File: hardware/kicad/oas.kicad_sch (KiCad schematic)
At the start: 0 parts

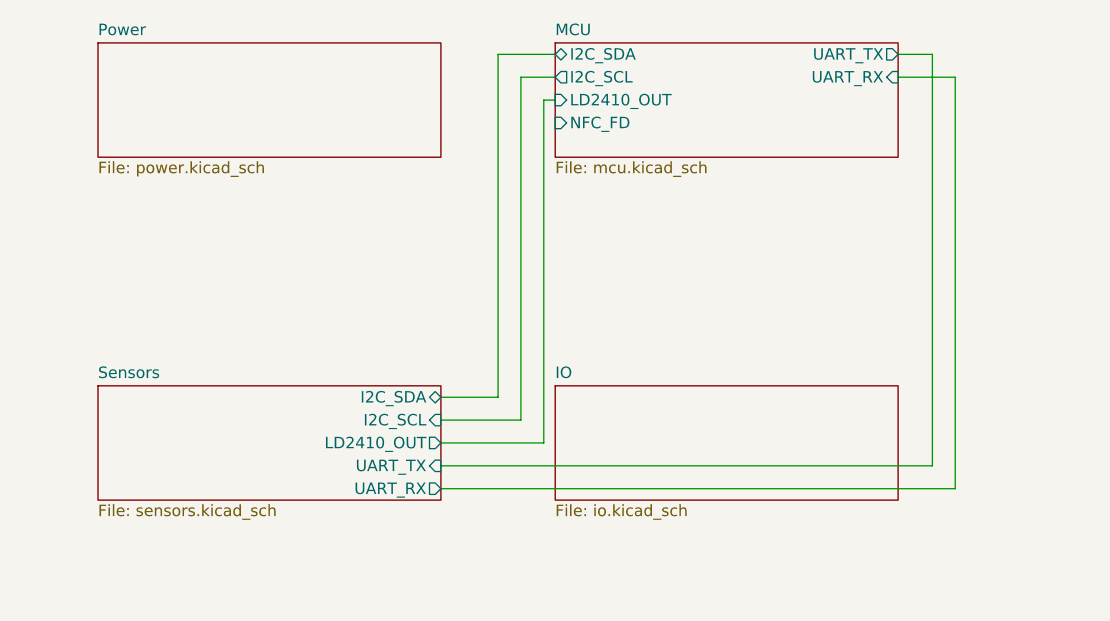
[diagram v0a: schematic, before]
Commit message: kicad: chunk #5c - MIKROE-2462 NFC Tag 2 Click (U4 + C12)
Final sensors-sub-sheet chunk: the NFC tag connection. Closes the
last expected ERC hier-label warning (NFC_FD).

Architecture change vs the v0.6 plan (a discrete NXP NT3H2x11 SMD +
custom PCB-trace NFC antenna): we instead host the NFC tag on a
MikroElektronika "NFC Tag 2 Click" (MIKROE-2462) -- NT3H2111 NTAG
I2C plus + onboard pre-tuned PCB antenna + mikroBUS 2x8 male header.
The Click board plugs into a 2x8 female pin socket on the OAS PCB
(P2.54 mm). Pre-tuned antenna eliminates the NXP AN11203 antenna-
design sub-project entirely; mikroBUS form factor is easy to source
(TME / Distrelec / Farnell / RS in the EU) and easy to swap or
remove for service via the pin-only mating.

Research summary (May 2026) drove the choice:
- MIKROE-2462 (NT3H2111 + antenna, mikroBUS, ~12-15 USD): selected.
- MIKROE-3659 (ST25DV16K, mikroBUS): strong runner-up; better EU
  stock but less DIY/ESPHome precedent.
- M5Stack U216, DFRobot DFR0231: rejected -- both are NFC readers
  (ST25R3916, PN532), not writeable tags.
- Adafruit NTAG I2C breakout: confirmed non-existent in catalog.
- Generic AliExpress NT3H2x11 breakouts: no citable listing meeting
  the Module Identification rule.

Schematic content (sensors.kicad_sch):
  U4 = Connector_Generic:Conn_02x08_Top_Bottom (placeholder for the
       mikroBUS socket; PCB footprint = 2x8 female pin socket P2.54
       mm, lands in chunk #7). The Top_Bottom variant of Conn_02x08
       has pins 1-8 down the LEFT column and 9-16 down the RIGHT
       column, exactly matching the mikroBUS pin-numbering convention.
       Only 6 pins are connected (the other 10 get no_connect markers):
         mikroBUS  7 (+3.3V) -> +3V3 power flag
         mikroBUS  8 (GND)   -> GND power flag
         mikroBUS 10 (INT)   -> NFC_FD hier label (output direction)
                                going to MCU GPIO 3
         mikroBUS 13 (SCL)   -> I2C_SCL hier label
         mikroBUS 14 (SDA)   -> I2C_SDA 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
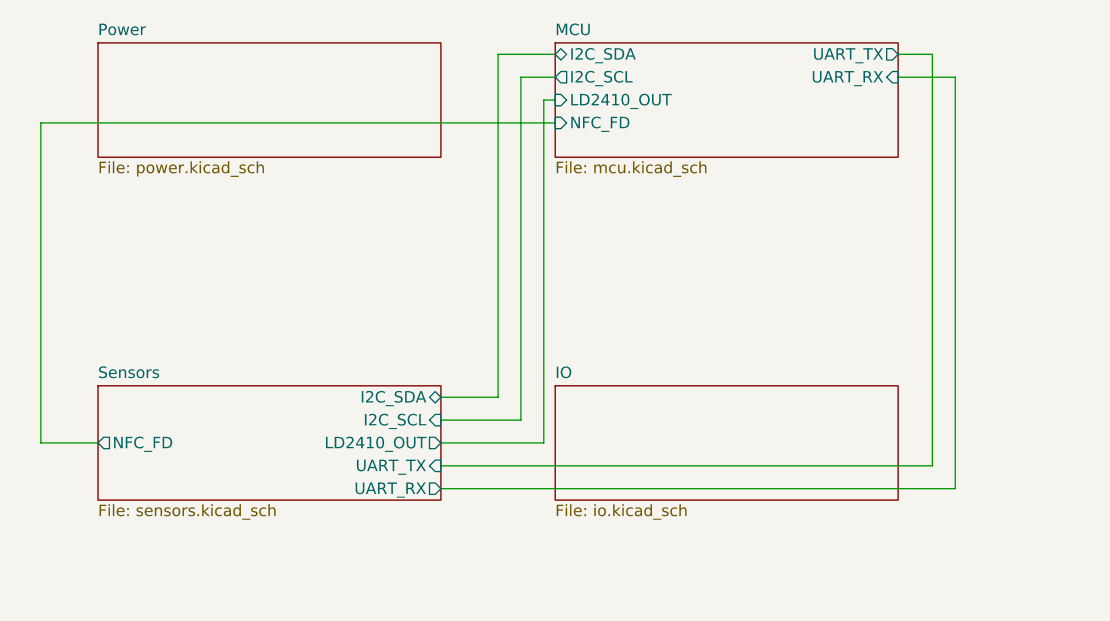
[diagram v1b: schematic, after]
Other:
- sheet Sensors ports: added NFC_FD; removed none
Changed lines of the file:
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@@
+			)
+		)
+		(pin "NFC_FD" output
+			(at 50.8 95.25 180)
+			(effects
+				(font
+					(size 1.27 1.27)
+				)
+				(justify right)
 			)
 		)
@@
 	)
 	(stroke
+		(width 0)
+		(type default)
+	)
+)
+(wire
+	(pts
+		(xy 50.8 95.25) (xy 44.45 95.25)
+	)
+	(stroke
+		(width 0)
+		(type default)
+	)
+)
+(wire
+	(pts
+		(xy 44.45 95.25) (xy 44.45 59.69)
+	)
+	(stroke
+		(width 0)
+		(type default)
+	)
+)
+(wire
+	(pts
+		(xy 44.45 59.69) (xy 101.6 59.69)
+	)
+	(stroke

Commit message: kicad+docs: v0.16 - AQI status LED ring (12 x SK6812-SIDE) + resolve OPEN ISSUE #2
Builds the side-emit RGB halo around the central cable hole: 12 SK6812 SIDE-A
LEDs on a Ø22 mm pitch circle (PCB origin = cable hole centre), each oriented
to emit radially OUTWARD into the AK-N-94 perforated cover. Per
hardware/components/_research-led-diffuse-ring.md the side-emit geometry
eliminates the "dot through perforation" problem at the structural level —
the cover never sees the die in line-of-sight.

Pinout verified twice (Normand SK6812 SIDE-A 2018 rev 01 + OPSCO SK6812
SIDE-A-001 2021 rev A/1, both via WebFetch + pdftotext): 1=DIN, 2=VDD,
3=DOUT, 4=GND. This differs from KiCad's stock LED:SK6812 symbol (which
is the PLCC4 5050 variant with 1=VSS/2=DIN/3=VDD/4=DOUT) — OAS ships its
own OAS:SK6812-SIDE symbol and oas:SK6812-SIDE footprint to avoid that
pitfall. Full part spec in hardware/components/sk6812-side.md.

Schematic additions (sensors.kicad_sch):
- 12 × D11..D22 OAS:SK6812-SIDE instances + 12 × C20..C31 Device:C 100 nF
  decoupling caps, vertical stack at X=40.64 with 25.4 mm row pitch.
- Daisy chain DIN→DOUT via 5-segment L-routes that bypass each LED body
  (avoids the spurious DIN↔DOUT short that a horizontal pass-through
  wire would create).
- D11 DIN driven from the new WS2812_DIN hierarchical label.
- D22 DOUT terminated with a no_connect.

Schematic / inter-sheet plumbing:
- mcu.kicad_sch: GPIO 8 (J1.9) moved from no-connect to signal pins.
  New WS2812_DIN hier label on the LEFT edge at the GPIO 8 pin row.
- SUBSHEET_PINS adds WS2812_DIN on the MCU and Sensors LEFT edges.
- Root sheet adds an inter-sheet wire at X = 41.91 (one grid step west
  of the existing NFC_FD vertical) joining the two new sheet pins.

PCB additions (oas.kicad_pcb):
- 12 × SK6812-SIDE footprints placed at θ = 0°..330° (30° steps) on the
  Ø22 mm pitch circle, each rotated to (270 - θ) so its body-local -Y
  (emission face) points radially outward.
- 12 × 100 nF 0402 caps, placed rad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
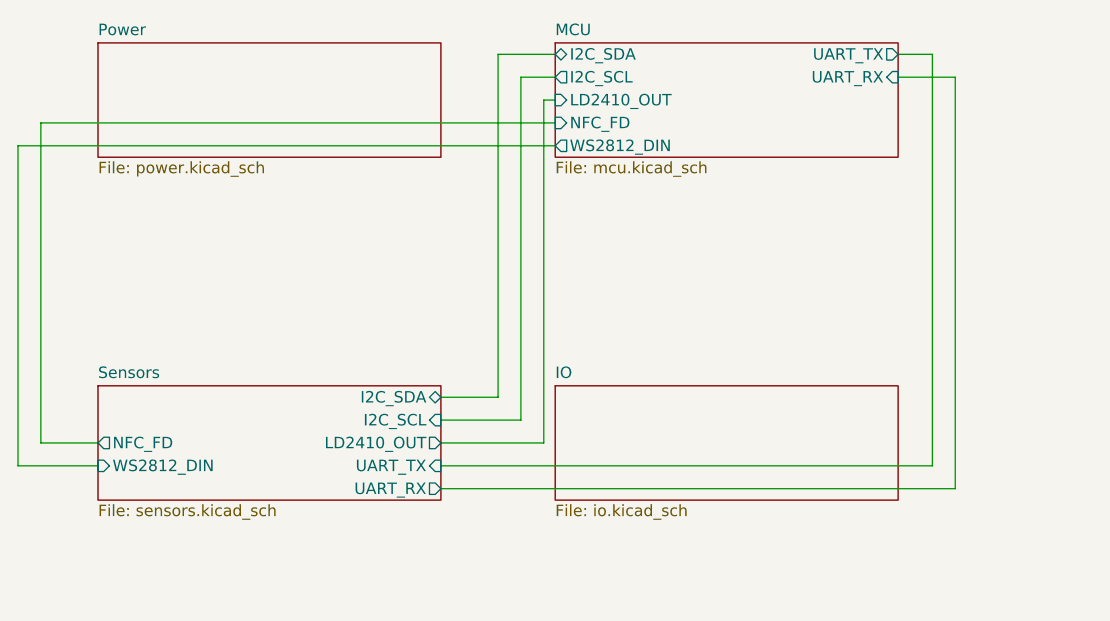
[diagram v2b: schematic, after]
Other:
- sheet MCU ports: added WS2812_DIN; removed none
- sheet Sensors ports: added WS2812_DIN; removed none
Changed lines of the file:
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@@
+			)
+		)
+		(pin "WS2812_DIN" output
+			(at 101.6 62.23 180)
+			(effects
+				(font
+					(size 1.27 1.27)
+				)
+				(justify right)
 			)
 		)
@@
 			)
 		)
+		(pin "WS2812_DIN" input
+			(at 50.8 97.79 180)
+			(effects
+				(font
+					(size 1.27 1.27)
+				)
+				(justify right)
+			)
+		)
 		(instances
 			(project "oas"
@@
 	)
 	(stroke
+		(width 0)
+		(type default)
+	)
+)
+(wire
+	(pts
+		(xy 50.8 97.79) (xy 41.91 97.79)
+	)
+	(stroke
+		(width 0)
+		(type default)
+	)
+)
+(wire
+	(pts
+		(xy 41.91 97.79) (xy 41.91 62.23)
+	)
+	(stroke
+		(width 0)
+		(type default)
+	)
+)
+(wire
+	(pts
+		(xy 41.91 62.23) (xy 101.6 62.23)
+	)
+	(stroke

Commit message: kicad+docs: v0.19 - IO sub-sheet populated (J9 Qwiic + J10 native-USB recovery DNP)
Closes review Mi4 ("IO sub-sheet still empty"). Implements both connectors
listed in CLAUDE.md as "tentative" since v0.1:

J9 - Qwiic / Stemma QT expansion (always populated)
  Stock JST_SH SM04B-SRSS-TB 4-pin horizontal SMD socket on cutout C5.
  Cable mouth faces the chord so the cable plugs in from outside the
  case. Pinout: GND / +3.3V / SDA / SCL — taps the shared I2C bus
  (SEN66 + NT3H1101 + Qwiic chain). I2C_SDA / I2C_SCL hier labels
  match the MCU exports.

J10 - Native-USB recovery header (DNP)
  Stock 6-pin 2.54 mm vertical THT pin header on cutout C3. Pads
  only — solder a header for emergency reflashing if both DevKitM-1
  on-module USB-C ports are damaged. Pinout (chord side → PCB
  interior): GND / +3V3 / USB_DM (GPIO 12) / USB_DP (GPIO 13) /
  EN (chip reset) / BOOT (GPIO 9 strap).

Cutout C4 reserved as v2 expansion placeholder (no connector).

Key plumbing changes:
  - GPIO 12 / GPIO 13 moved from ESP32C6_DEVKITM1_NC_PINS to
    ESP32C6_DEVKITM1_SIGNAL_PIN as USB_DM / USB_DP. MCU sheet now
    wires U3.28 / U3.29 east to hier labels.
  - EN / BOOT migrated from MCU sub-sheet local labels to hier
    labels so the same nets reach the IO sheet's J10.5 / J10.6.
    J2_PIN_MAP[5] "RST" -> "EN".
  - CUTOUTS extended with allow_pads bool; C3 and C5 flip the
    copper keepout zone's pads-not-allowed rule so connector pads
    can live inside the case-wall opening.
  - SUBSHEET_SIZE bumped to (38.1, 17.78) for 6 pins per edge.
  - Root sheet inter-sheet wires extended for I2C bus → IO + new
    routes for USB_DM/USB_DP/EN/BOOT (MCU right ↔ IO left).
  - _emit_stock_lib_footprint() factored out the parse-and-patch
    logic shared by gen_j1/j3/j4 footprint generators; gen_j9 and
    gen_j10 are thin wrappers around it.

DRC = 0, ERC = 0.

BOM impact: +1 SKU (JST SM04B-SRSS-TB, ~€0.50). J10 pin header is
DNP — 0 BOM lines for the production assembly.

Co-Authored-By: Clau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
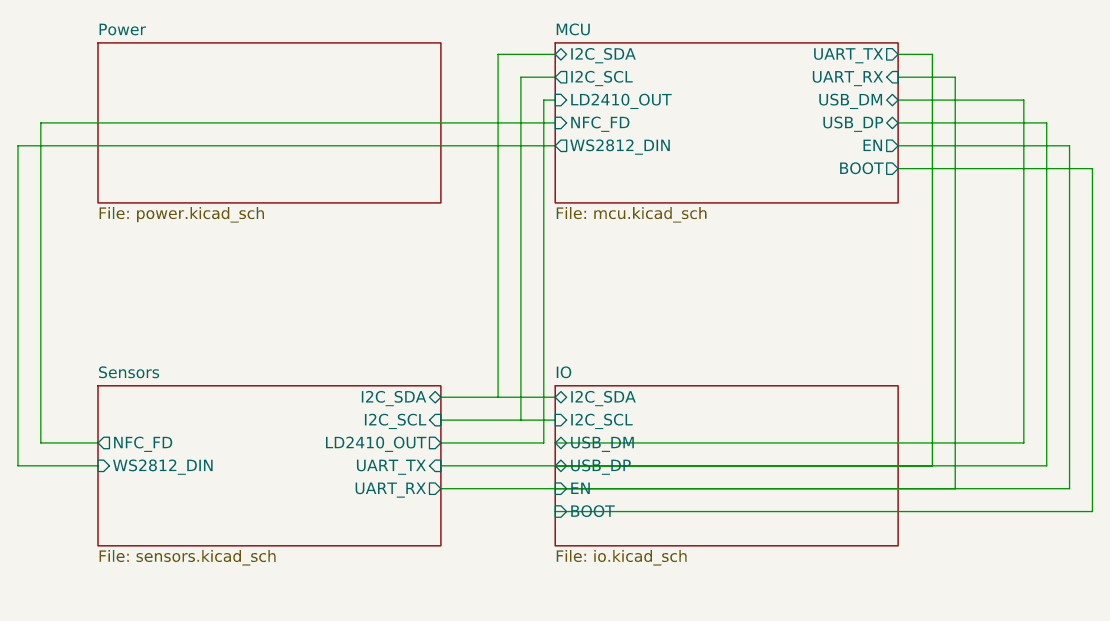
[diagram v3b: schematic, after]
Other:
- sheet IO ports: added BOOT, EN, I2C_SCL, I2C_SDA, USB_DM, USB_DP; removed none
- sheet MCU ports: added BOOT, EN, USB_DM, USB_DP; removed none
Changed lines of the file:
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@@
 	(sheet
 		(at 50.8 50.8)
-		(size 38.1 12.7)
+		(size 38.1 17.78)
 		(exclude_from_sim no)
 		(in_bom yes)
@@
 		)
 		(property "Sheetfile" "power.kicad_sch"
-			(at 50.8 63.9446 0)
+			(at 50.8 69.0246 0)
 			(effects
 				(font
@@
 	(sheet
 		(at 101.6 50.8)
-		(size 38.1 12.7)
+		(size 38.1 17.78)
 		(exclude_from_sim no)
 		(in_bom yes)
@@
 		)
 		(property "Sheetfile" "mcu.kicad_sch"
-			(at 101.6 63.9446 0)
+			(at 101.6 69.0246 0)
 			(effects
 				(font
@@
 		(pin "UART_RX" input
 			(at 139.7 54.61 0)
+			(effects
+				(font
+					(size 1.27 1.27)
+				)
+				(justify left)
+			)
+		)
+		(pin "USB_DM" bidirectional
+			(at 139.7 57.15 0)
+			(effects
+				(font
+					(size 1.27 1.27)
+				)
+				(justify left)
+			)
+		)
+		(pin "USB_DP" bidirectional
+			(at 139.7 59.69 0)
+			(effects
+				(font
+					(size 1.27 1.27)
+				)
+				(justify left)
+			)
+		)
+		(pin "EN" output
+			(at 139.7 62.23 0)
+			(effects
+				(font
+					(size 1.27 1.27)
+				)
+				(justify left)
+			)
+		)
+		(pin "BOOT" output
+			(at 139.7 64.77 0)
 			(effects
 				(font
@@
 	(sheet
 		(at 50.8 88.9)
-		(size 38.1 12.7)
+		(size 38.1 17.78)
 		(exclude_from_sim no)
 		(in_bom yes)
@@
 		)
 		(property "Sheetfile" "sensors.kicad_sch"
-			(at 50.8 102.0446 0)
+			(at 50.8 107.1246 0)
 			(effects
 				(font
@@
 	(sheet
 		(at 101.6 88.9)
-		(size 38.1 12.7)
+		(size 38.1 17.78)
 		(exclude_from_sim no)
 		(in_bom yes)
@@
 		)
 		(property "Sheetfile" "io.kicad_sch"
-			(at 101.6 102.0446 0)
+			(at 101.6 107.1246 0)
 			(effects
 				(font
@@
 				)
 				(justify left top)
+			)
+		)
+		(pin "I2C_SDA" bidirectional
+			(at 101.6 90.17 180)
+			(effects
+				(font
+					(size 1.27 1.27)
+				)
+				(justify right)
+			)
+		)
+		(pin "I2C_SCL" input
+			(at 101.6 92.71 180)
+			(effects
+				(font
+					(size 1.27 1.27)
+				)
+				(justify right)
+			)
+		)
+		(pin "USB_DM" bidirectional
+			(at 101.6 95.25 180)
+			(effects
+				(font
+					(size 1.27 1.27)
+				)
+				(justify right)
+			)
+		)
+		(pin "USB_DP" bidirectional
+			(at 101.6 97.79 180)
+			(effects
+				(font
+					(size 1.27 1.27)
+				)
+				(justify right)
+			)
+		)
+		(pin "EN" input
+			(at 101.6 100.33 180)
+			(effects
+				(font
+					(size 1.27 1.27)
+				)
+				(justify right)
+			)
+		)
+		(pin "BOOT" input
+			(at 101.6 102.87 180)
+			(effects
+				(font
+					(size 1.27 1.27)
+				)
+				(justify right)
 			)
 		)
@@
 	)
 	(stroke
+		(width 0)
+		(type default)
+	)
+)
+(wire
+	(pts
+		(xy 95.25 90.17) (xy 101.6 90.17)
+	)
+	(stroke
+		(width 0)
+		(type default)
+	)
+)
+(wire
+	(pts
+		(xy 97.79 92.71) (xy 101.6 92.71)
+	)
+	(stroke
+		(width 0)
+		(type default)
+	)
+)
+(wire
+	(pts
+		(xy 139.7 57.15) (xy 153.67 57.15)
+	)
+	(stroke
+		(width 0)
+		(type default)
+	)
+)
+(wire
+	(pts
+		(xy 153.67 57.15) (xy 153.67 95.25)
+	)
+	(stroke
+		(width 0)
+		(type default)
+	)
+)
+(wire
+	(pts
+		(xy 153.67 95.25) (xy 101.6 95.25)
+	)
+	(stroke
+		(width 0)
+		(type default)
+	)
+)
+(wire
+	(pts
+		(xy 139.7 59.69) (xy 156.21 59.69)
+	)
+	(stroke
+		(width 0)
+		(type default)
+	)
+)
+(wire
+	(pts
+		(xy 156.21 59.69) (xy 156.21 97.79)
+	)
+	(stroke
+		(width 0)
+		(type default)
+	)
+)
+(wire
+	(pts
+		(xy 156.21 97.79) (xy 101.6 97.79)
+	)
+	(stroke
+		(width 0)
+		(type default)
+	)
+)
+(wire
+	(pts
+		(xy 139.7 62.23) (xy 158.75 62.23)
+	)
+	(stroke
+		(width 0)
+		(type default)
+	)
+)
+(wire
+	(pts
+		(xy 158.75 62.23) (xy 158.75 100.33)
+	)
+	(stroke
+		(width 0)
+		(type default)
+	)
+)
+(wire
+	(pts
+		(xy 158.75 100.33) (xy 101.6 100.33)
+	)
+	(stroke
+		(width 0)
+		(type default)
+	)
+)
+(wire
+	(pts
+		(xy 139.7 64.77) (xy 161.29 64.77)
+	)
+	(stroke
+		(width 0)
+		(type default)
+	)
+)
+(wire
+	(pts
+		(xy 161.29 64.77) (xy 161.29 102.87)
+	)
+	(stroke
+		(width 0)
+		(type default)
+	)
+)
+(wire
+	(pts
+		(xy 161.29 102.87) (xy 101.6 102.87)
+	)
+	(stroke

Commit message: kicad+docs: v0.21 - M3 closure (J5/J6/J7/J8 schematic) + UART/USB crossover fix
M3 part 1 (MCU): replace U3 placeholder with J5 + J6 schematic symbols
(Conn_01x15 each). J5 = ESP32 J1 antenna-side row (pin tips left,
angle=0); J6 = ESP32 J3 USB-side row (pin tips right, angle=180). Pin
numbers 1..15 match PCB pad numbering 1:1. All 7 OAS signal pins get
hier-label stubs; 5 GND pins get power flags; 13 NC pins get
no_connect markers. J2 DNP recovery header rotated 180 so its TX/RX
pin row aligns with J6 UART_TX/RX.

M3 part 2 (Sensors): replace U4 mikroBUS placeholder with J7 + J8
schematic symbols (Conn_01x08 each). J7 = mikroBUS pins 1..8 (LEFT
column, angle=0); J8 = mikroBUS pins 9..16 (RIGHT column, angle=180).
J7 pin 7 = +3V3, J7 pin 8 = GND, J8 pin 2 = NFC_FD, J8 pin 5 = SCL,
J8 pin 6 = SDA, J8 pin 8 = GND; 10 unused pins get no_connect markers.

Root-sheet UART/USB crossover bug fixed (pre-existing v0.20 finding):
the UART_TX east-from-sensors wire ran at Y=97.79 in the same column
as the IO sub-sheet's USB_DP west-into-io wire (also at Y=97.79),
overlapping in X range [101.6, 143.51] and bridging UART_TX into
USB_DP. Same pattern for UART_RX/EN at Y=100.33. Fix re-routes UART
east stubs south of the IO block before going east (Y=110.49 for
UART_TX, Y=113.03 for UART_RX), eliminating the Y collision. Verified
clean: /MCU/UART_TX = {J2.3, J4.3, J6.2}, /MCU/UART_RX = {J2.4, J4.2,
J6.3}, /IO/USB_DP / EN no longer contain LD2410 or UART pins.

SEN66 mech-ref F.CrtYd removed (5 of 15 v0.20 DRC violations were
false-positive courtyards_overlap between SENS1 body and PCB-surface
SMD parts; SEN66 floats 21.5 mm above PCB so the 2D courtyard rule
doesn't reflect physical clearance). Matches the existing convention
in _emit_daughterboard_reference_pcb_footprint() (MOD1/MOD2).

Net coverage: 216 pad-net assignments applied by
sync_pcb_nets_from_schematic (up from 188 in v0.20). All J5..J8
sockets fully assigned. DRC: 10 violations (down from 15) - 1
courtyards_overlap C4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
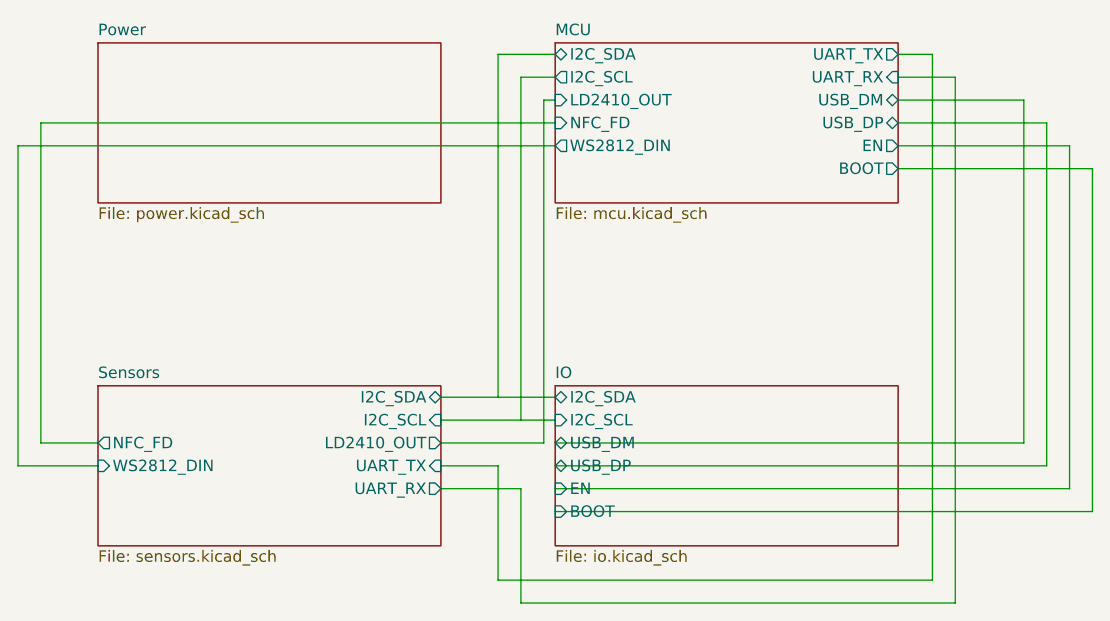
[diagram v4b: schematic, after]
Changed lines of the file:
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@@
 (wire
 	(pts
-		(xy 88.9 97.79) (xy 143.51 97.79)
+		(xy 88.9 97.79) (xy 95.25 97.79)
 	)
 	(stroke
@@
 (wire
 	(pts
-		(xy 143.51 97.79) (xy 143.51 52.07)
+		(xy 95.25 97.79) (xy 95.25 110.49)
+	)
+	(stroke
+		(width 0)
+		(type default)
+	)
+)
+(wire
+	(pts
+		(xy 95.25 110.49) (xy 143.51 110.49)
+	)
+	(stroke
+		(width 0)
+		(type default)
+	)
+)
+(wire
+	(pts
+		(xy 143.51 110.49) (xy 143.51 52.07)
 	)
 	(stroke
@@
 (wire
 	(pts
-		(xy 88.9 100.33) (xy 146.05 100.33)
+		(xy 88.9 100.33) (xy 97.79 100.33)
 	)
 	(stroke
@@
 (wire
 	(pts
-		(xy 146.05 100.33) (xy 146.05 54.61)
+		(xy 97.79 100.33) (xy 97.79 113.03)
 	)
 	(stroke
+		(width 0)
+		(type default)
+	)
+)
+(wire
+	(pts
+		(xy 97.79 113.03) (xy 146.05 113.03)
+	)
+	(stroke
+		(width 0)
+		(type default)
+	)
+)
+(wire
+	(pts
+		(xy 146.05 113.03) (xy 146.05 54.61)
+	)
+	(stroke
